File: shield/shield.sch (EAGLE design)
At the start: 4 parts, among them IC1 LM73

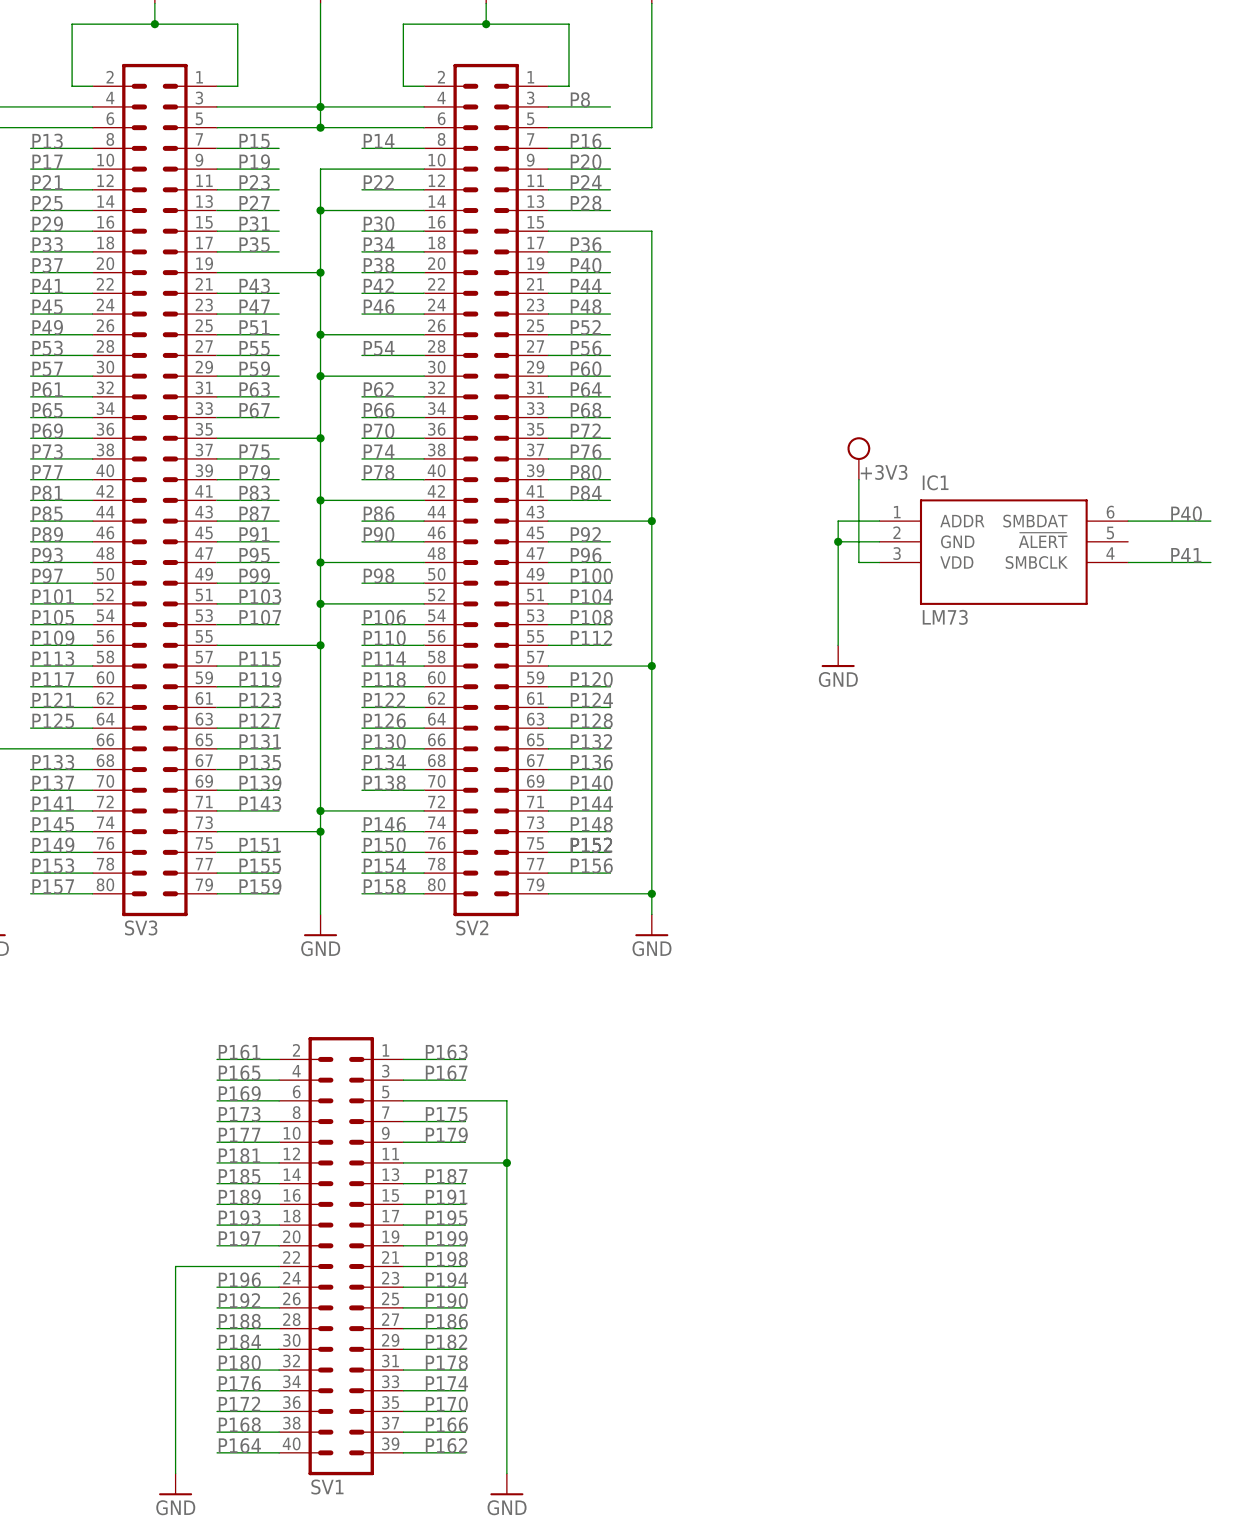
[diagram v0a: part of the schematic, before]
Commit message: remove lm73 from shield
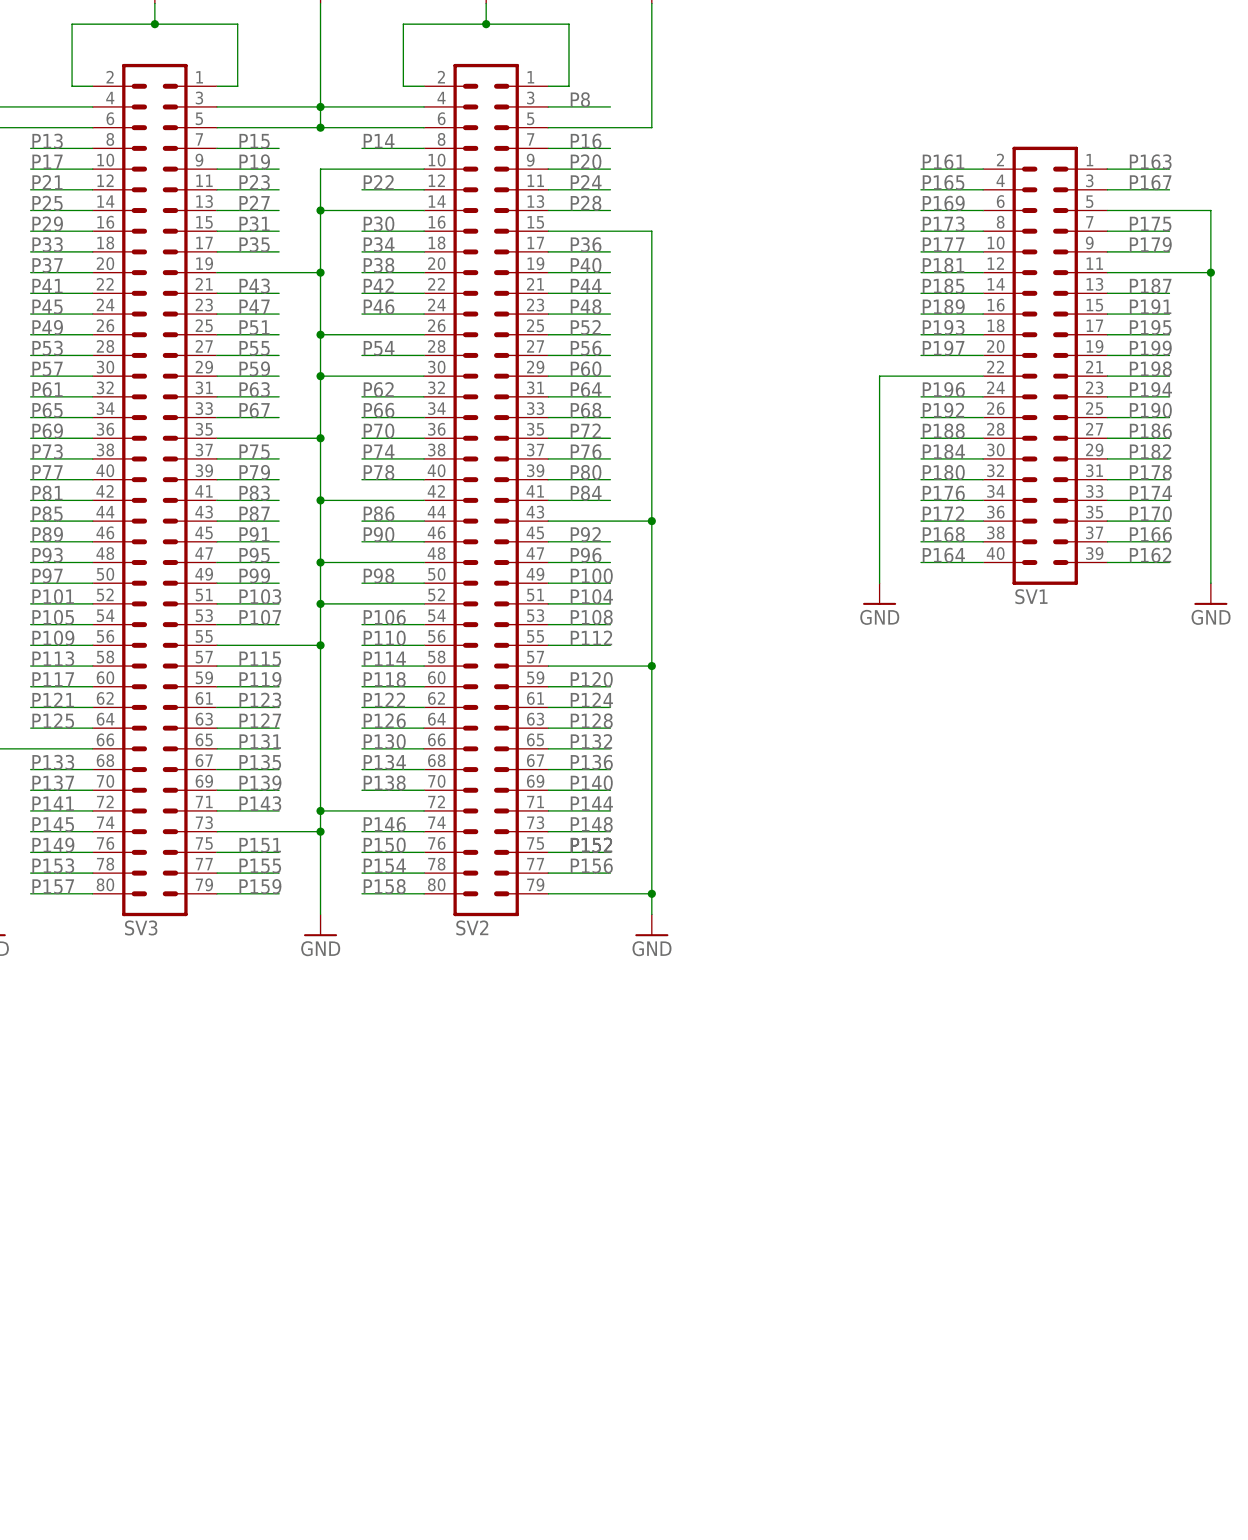
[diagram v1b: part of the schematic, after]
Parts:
- removed IC1: LM73, boomerang:LM73
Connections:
- net +3V3: no longer IC1.VDD
- net GND: no longer IC1.ADDR, IC1.GND
- net P40: no longer IC1.SMBDAT
- net P41: no longer IC1.SMBCLK
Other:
- moved on the sheet: SV1

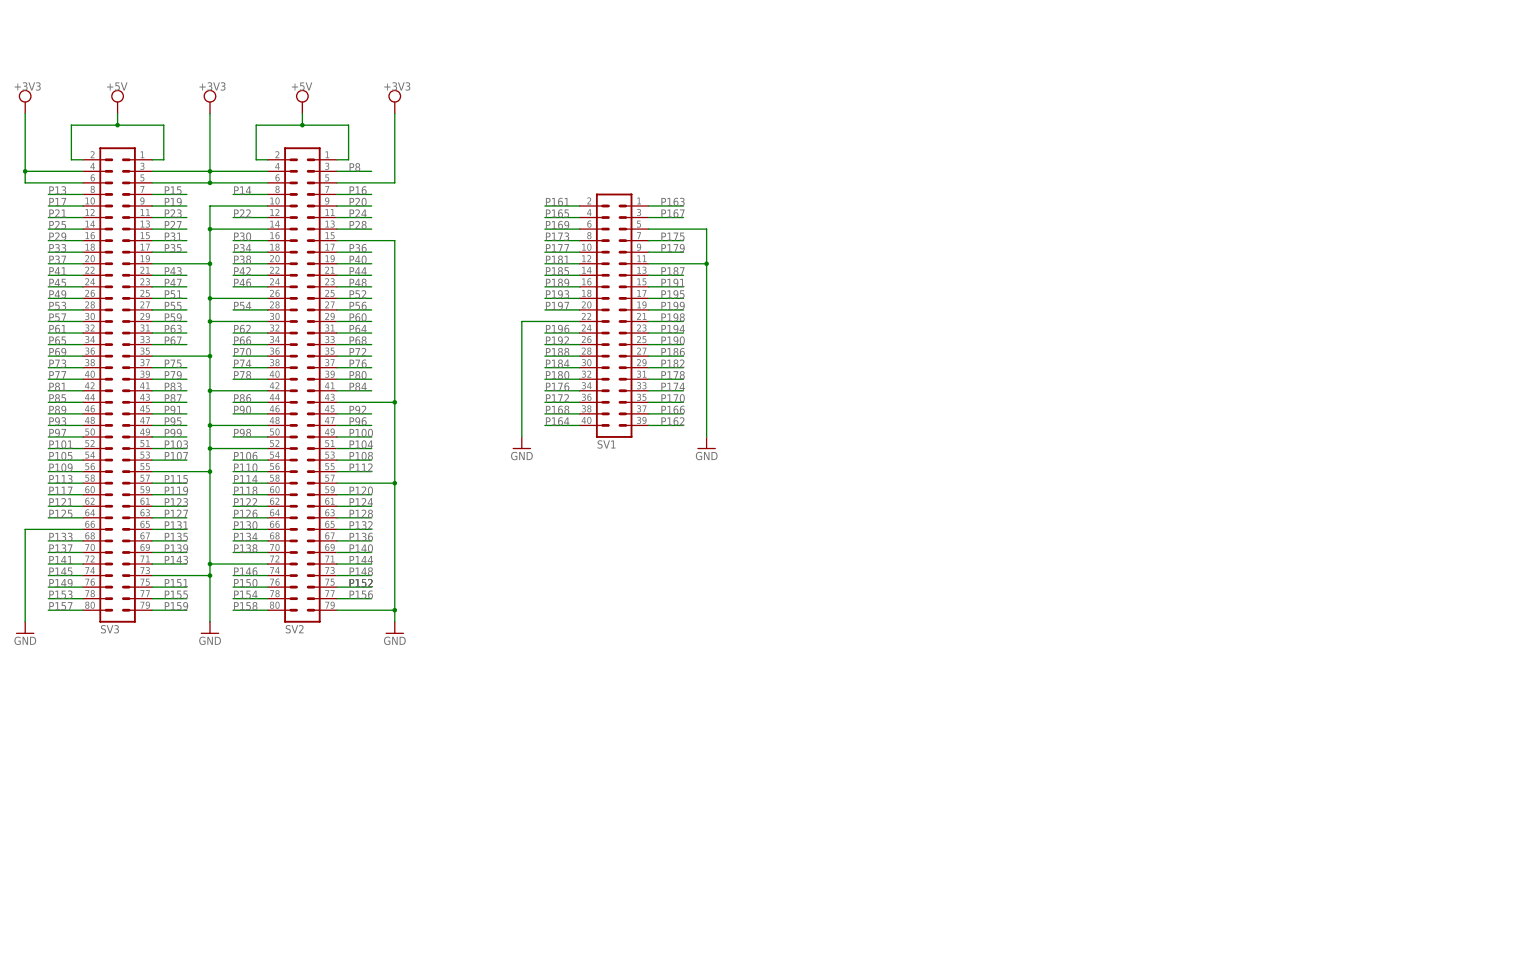
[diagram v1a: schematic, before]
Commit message: Update schield schematic
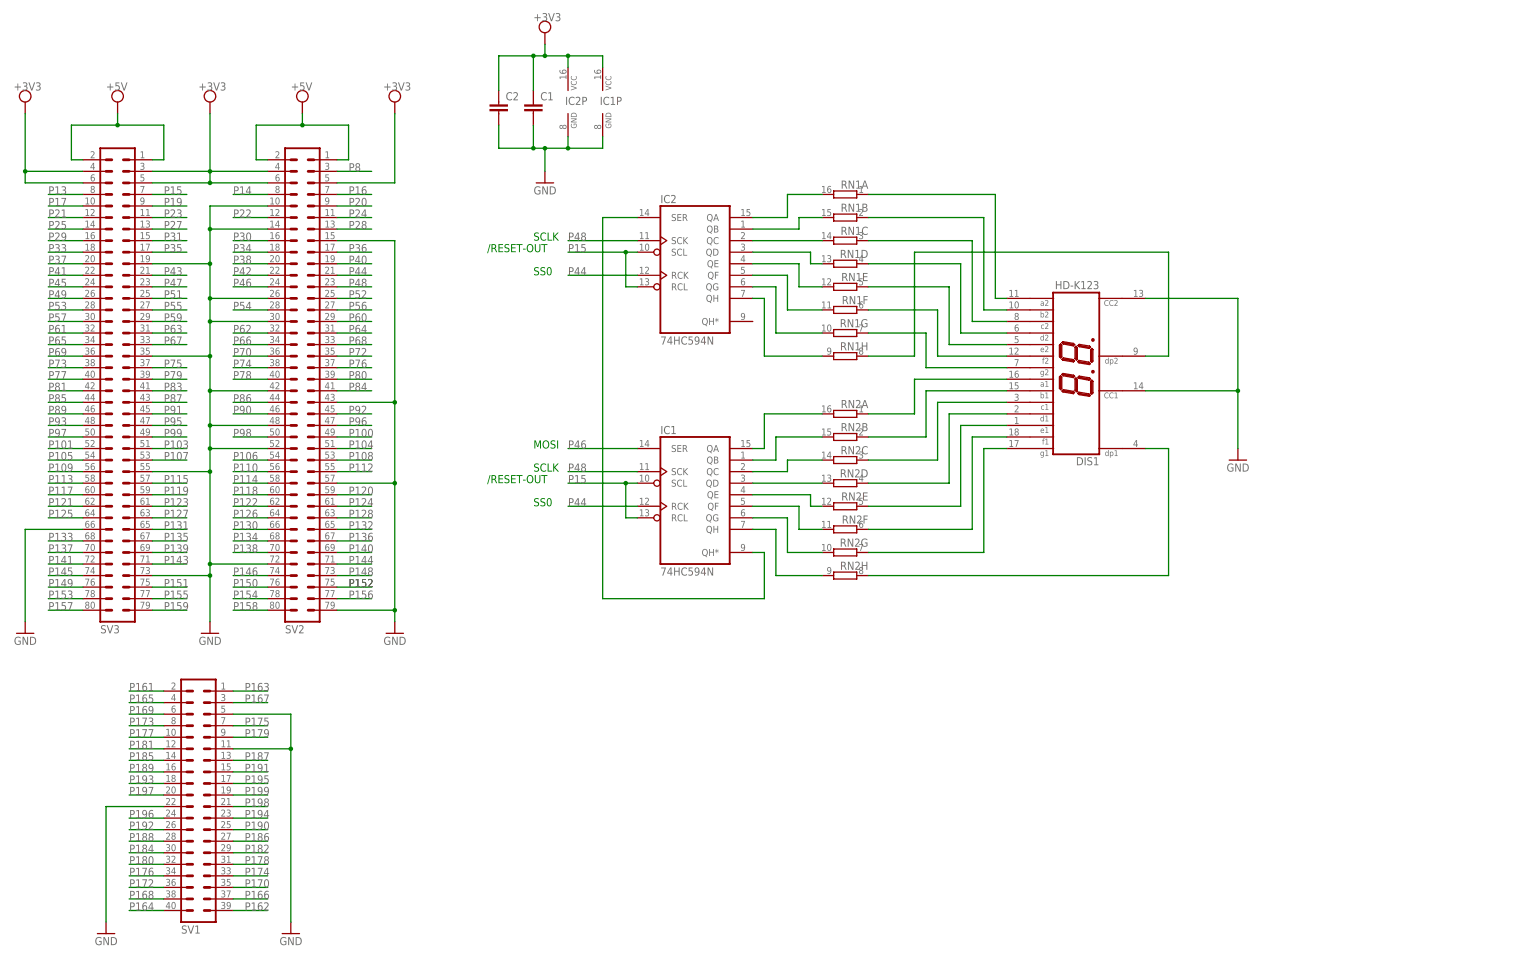
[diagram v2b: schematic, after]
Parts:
- added C1, C2: (no value), rcl:C-EU025-030X050
- added DIS1: HD-K123, display-hp:HD-K123
- added IC1, IC2: 74HC594N, 74xx-eu:74HC594N
- added RN1, RN2: (no value), resistor-dil:8R-N
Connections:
- new net N$1: IC2A.QA, RN1A.2
- new net N$10: IC1A.QB, RN2B.2
- new net N$11: IC1A.QC, RN2C.2
- new net N$12: IC1A.QD, RN2D.2
- new net N$13: IC1A.QE, RN2E.2
- new net N$14: IC1A.QF, RN2F.2
- new net N$15: IC1A.QG, RN2G.2
- new net N$16: IC1A.QH, RN2H.2
- new net N$17: IC1A.QH*, IC2A.SER
- new net N$18: DIS1.A2, RN1A.1
- new net N$19: DIS1.B2, RN1B.1
- new net N$2: IC2A.QB, RN1B.2
- new net N$20: DIS1.C2, RN1C.1
- new net N$21: DIS1.D2, RN1D.1
- new net N$22: DIS1.E2, RN1E.1
- new net N$23: DIS1.F2, RN1F.1
- new net N$24: DIS1.G2, RN1G.1
- new net N$25: DIS1.G1, RN2G.1
- new net N$26: DIS1.A1, RN2A.1
- new net N$27: DIS1.B1, RN2B.1
- new net N$28: DIS1.C1, RN2C.1
- new net N$29: DIS1.D1, RN2D.1
- new net N$3: IC2A.QC, RN1C.2
- new net N$30: DIS1.E1, RN2E.1
- new net N$31: DIS1.F1, RN2F.1
- new net N$32: DIS1.DP2, RN1H.1
- new net N$33: DIS1.DP1, RN2H.1
- new net N$4: IC2A.QD, RN1D.2
- new net N$5: IC2A.QE, RN1E.2
- new net N$6: IC2A.QF, RN1F.2
- new net N$7: IC2A.QG, RN1G.2
- new net N$8: IC2A.QH, RN1H.2
- new net N$9: IC1A.QA, RN2A.2
- net +3V3: now also C1.1, C2.1, IC1P.VCC, IC2P.VCC
- net GND: now also C1.2, C2.2, DIS1.CC1, DIS1.CC2, IC1P.GND, IC2P.GND
- net P15: now also IC1A.RCL, IC1A.SCL, IC2A.RCL, IC2A.SCL
- net P44: now also IC1A.RCK, IC2A.RCK
- net P46: now also IC1A.SER
- net P48: now also IC1A.SCK, IC2A.SCK
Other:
- note added: "/RESET-OUT"
- note added: "MOSI"
- note added: "SCLK"
- note added: "SS0"
- moved on the sheet: SV1

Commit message: Update schematic
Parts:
- removed C2: (no value), rcl:C-EU025-030X050
- removed DIS1: HD-K123, display-hp:HD-K123
- removed IC1, IC2: 74HC594N, 74xx-eu:74HC594N
- removed RN1, RN2: (no value), resistor-dil:8R-N
- added DIS2: HD-K121, display-hp:HD-K121
- added U1: TLC5925IDWR, Texas Instruments_By_element14_Batch_1:TLC5925IDWR
- C1: value (none) -> 100n; device rcl:C-EU025-030X050 -> capacitor-wima:C2.5/2
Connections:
- removed net N$17: IC1A.QH*, IC2A.SER
- removed net N$18: DIS1.A2, RN1A.1
- removed net N$19: DIS1.B2, RN1B.1
- removed net N$20: DIS1.C2, RN1C.1
- removed net N$21: DIS1.D2, RN1D.1
- removed net N$22: DIS1.E2, RN1E.1
- removed net N$23: DIS1.F2, RN1F.1
- removed net N$24: DIS1.G2, RN1G.1
- removed net N$25: DIS1.G1, RN2G.1
- removed net N$26: DIS1.A1, RN2A.1
- removed net N$27: DIS1.B1, RN2B.1
- removed net N$28: DIS1.C1, RN2C.1
- removed net N$29: DIS1.D1, RN2D.1
- removed net N$30: DIS1.E1, RN2E.1
- removed net N$31: DIS1.F1, RN2F.1
- removed net N$32: DIS1.DP2, RN1H.1
- removed net N$33: DIS1.DP1, RN2H.1
- net +3V3: now also DIS2.CA1, DIS2.CA2, U1.VDD; no longer C2.1, IC1P.VCC, IC2P.VCC
- net GND: now also U1.GND; no longer C2.2, DIS1.CC1, DIS1.CC2, IC1P.GND, IC2P.GND
- net N$1: now also DIS2.E2, U1.~OUT0; no longer IC2A.QA, RN1A.2
- net N$10: now also DIS2.D1, U1.~OUT9; no longer IC1A.QB, RN2B.2
- net N$11: now also DIS2.G1, U1.~OUT10; no longer IC1A.QC, RN2C.2
- net N$12: now also DIS2.C1, U1.~OUT11; no longer IC1A.QD, RN2D.2
- net N$13: now also DIS2.DP1, U1.~OUT12; no longer IC1A.QE, RN2E.2
- net N$14: now also DIS2.B1, U1.~OUT13; no longer IC1A.QF, RN2F.2
- net N$15: now also DIS2.A1, U1.~OUT14; no longer IC1A.QG, RN2G.2
- net N$16: now also DIS2.F1, U1.~OUT15; no longer IC1A.QH, RN2H.2
- net N$2: now also DIS2.D2, U1.~OUT1; no longer IC2A.QB, RN1B.2
- net N$3: now also DIS2.G2, U1.~OUT2; no longer IC2A.QC, RN1C.2
- net N$4: now also DIS2.C2, U1.~OUT3; no longer IC2A.QD, RN1D.2
- net N$5: now also DIS2.DP2, U1.~OUT4; no longer IC2A.QE, RN1E.2
- net N$6: now also DIS2.B2, U1.~OUT5; no longer IC2A.QF, RN1F.2
- net N$7: now also DIS2.A2, U1.~OUT6; no longer IC2A.QG, RN1G.2
- net N$8: now also DIS2.F2, U1.~OUT7; no longer IC2A.QH, RN1H.2
- net N$9: now also DIS2.E1, U1.~OUT8; no longer IC1A.QA, RN2A.2
- net P15: no longer IC1A.RCL, IC1A.SCL, IC2A.RCL, IC2A.SCL
- net P44: no longer IC1A.RCK, IC2A.RCK
- net P46: now also U1.SDI; no longer IC1A.SER
- net P48: now also U1.CLK; no longer IC1A.SCK, IC2A.SCK
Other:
- note added: "0 E 1 D 2 G 3 C 4 P 5 B 6 1 7 F"
- note removed: "/RESET-OUT"
- note removed: "MOSI"
- note removed: "SCLK"
- note removed: "SS0"
- moved on the sheet: C1

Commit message: Update schematics
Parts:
- added IC1: LM75, lm75:LM75_ICN
- added Q1, Q2, Q3, Q4: BUZ11BV, transistor-power:BUZ11BV
- added R1, R2: 10k, rcl:R-EU_0207/10
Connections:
- new net N$17: Q1.S, Q2.S, Q3.S, Q4.S
- net +3V3: now also IC1.VCC, R1.2, R2.2
- net GND: now also IC1.A0, IC1.A1, IC1.A2, IC1.GND
- net P40: now also IC1.SDA, R2.1
- net P41: now also IC1.SCL, R1.1
- net P77: now also Q1.G
- net P78: now also Q2.G
- net P79: now also Q3.G
- net P80: now also Q4.G
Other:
- moved on the sheet: C1, DIS2, U1
